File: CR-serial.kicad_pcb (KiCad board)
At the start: 4 copper layers, 81.5 x 67.8 mm, 94 parts, among them J1 USB_B, J2 GPIO, J3 UART0, J4 UART1, J5 UART2, J6 UART3_HV, J7 RS232_0, J8 RS232_1, U1 CP2108-xxx-xM, U10 TVS4201MR6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

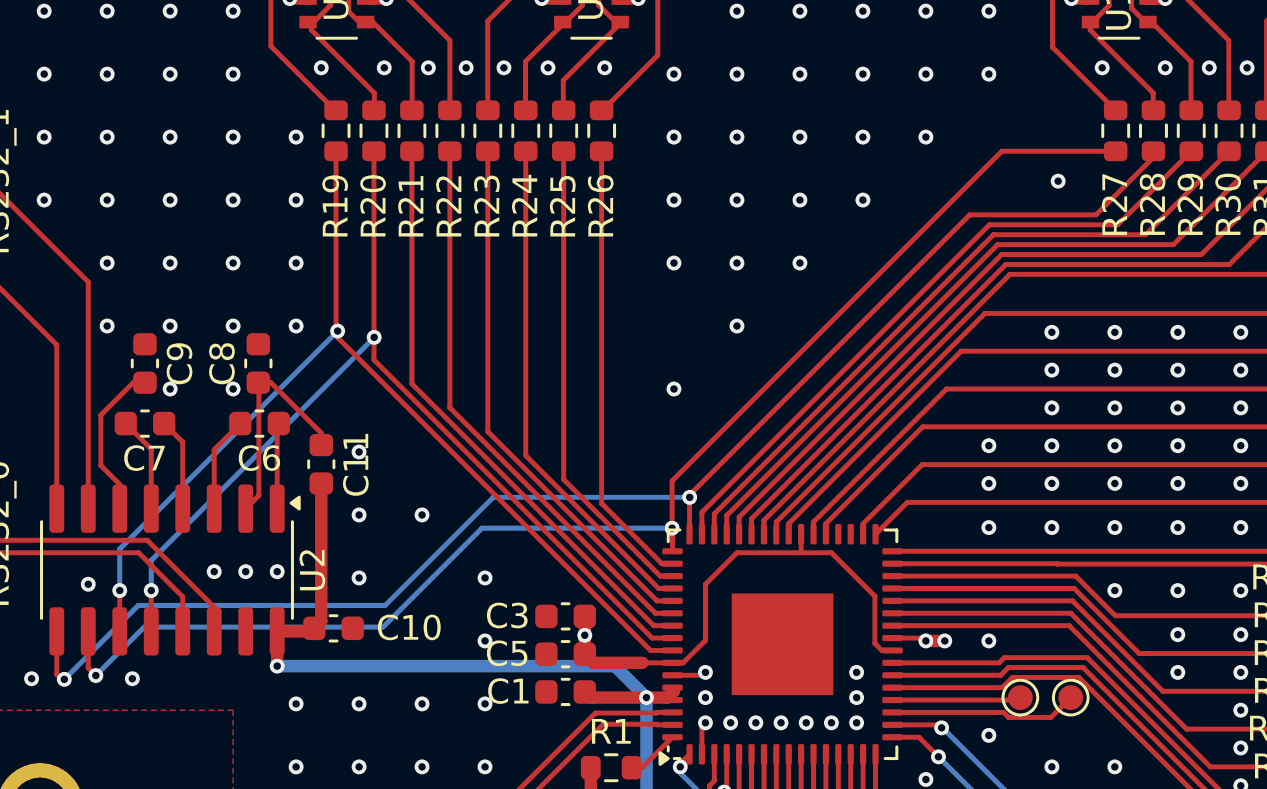
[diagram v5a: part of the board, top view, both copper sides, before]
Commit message: PCB: Add RS232 RX enable resistors, unfill zones
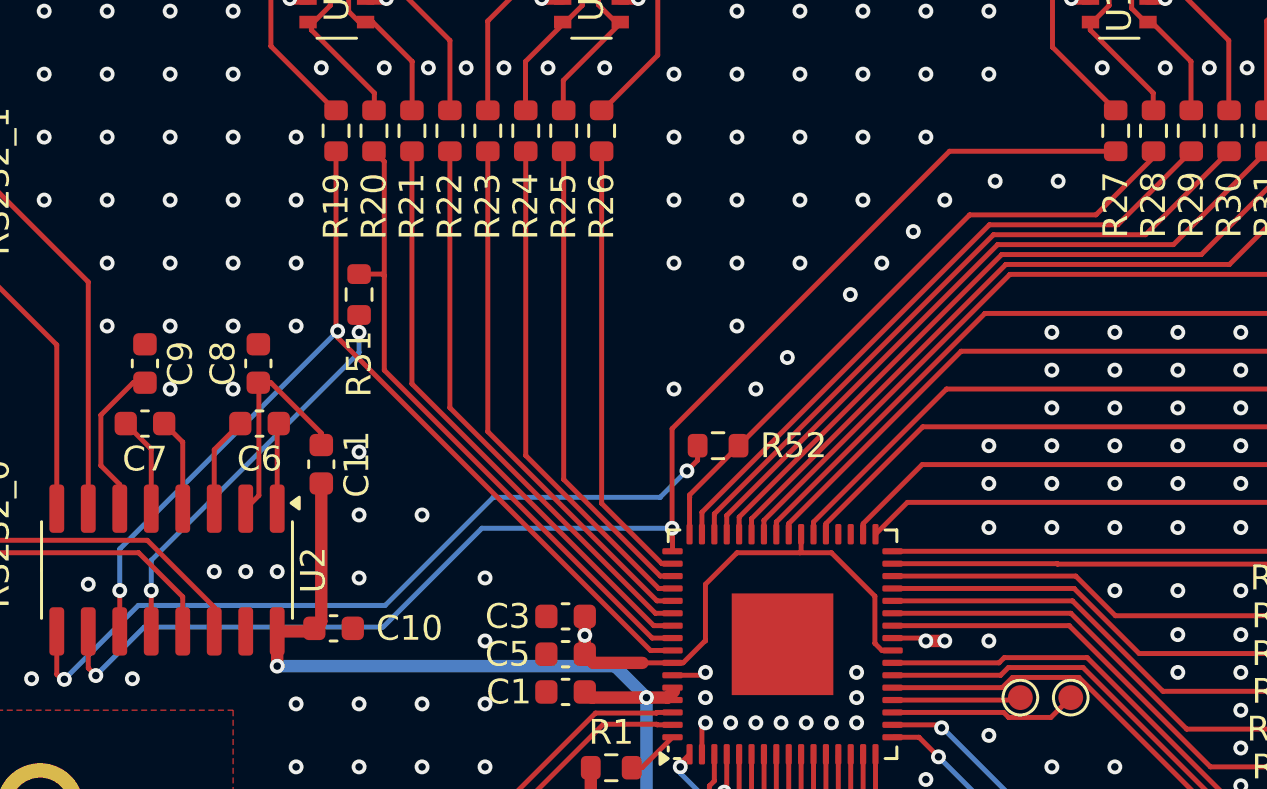
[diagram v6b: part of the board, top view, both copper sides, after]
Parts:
- added R51: 0R, Resistor_SMD:R_0603_1608Metric, F.Cu at (182.9, 102.9)
- added R52: 0R, Resistor_SMD:R_0603_1608Metric, F.Cu at (197.4, 109.0)
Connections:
- U2 pad 12: RX0 -> Net-(U2-R1OUT)
- U2 pad 9: RX1 -> Net-(U2-R2OUT)
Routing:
- net Net-(U2-R2OUT): track 0.00 -> 32.2 mm, vias 0 -> 2
- net RX1: track 56.8 -> 26.2 mm, vias 2 -> 0
- net Net-(U2-R1OUT): track 0.00 -> 16.2 mm, vias 0 -> 2
- net RX0: track 40.7 -> 26.1 mm, vias 2 -> 0
- net TX1: track 53.9 -> 55.1 mm
- net GND: vias 358 -> 365

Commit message: Add fiducials
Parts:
- added FID1: Fiducial, QCP_parts:Fiducial_Cross_0.5mm_Mask2mm, F.Cu at (171.4, 87.6)
- added FID2: Fiducial, QCP_parts:Fiducial_Cross_0.5mm_Mask2mm, F.Cu at (232.4, 95.2)
- added FID3: Fiducial, QCP_parts:Fiducial_Cross_0.5mm_Mask2mm, F.Cu at (171.4, 143.5)
